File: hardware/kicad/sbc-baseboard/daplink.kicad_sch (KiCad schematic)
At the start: 15 parts, among them J601 SWD (K20), SW601 DAP RESET, U601 MK20DX128VFM5, Y601 8MHz

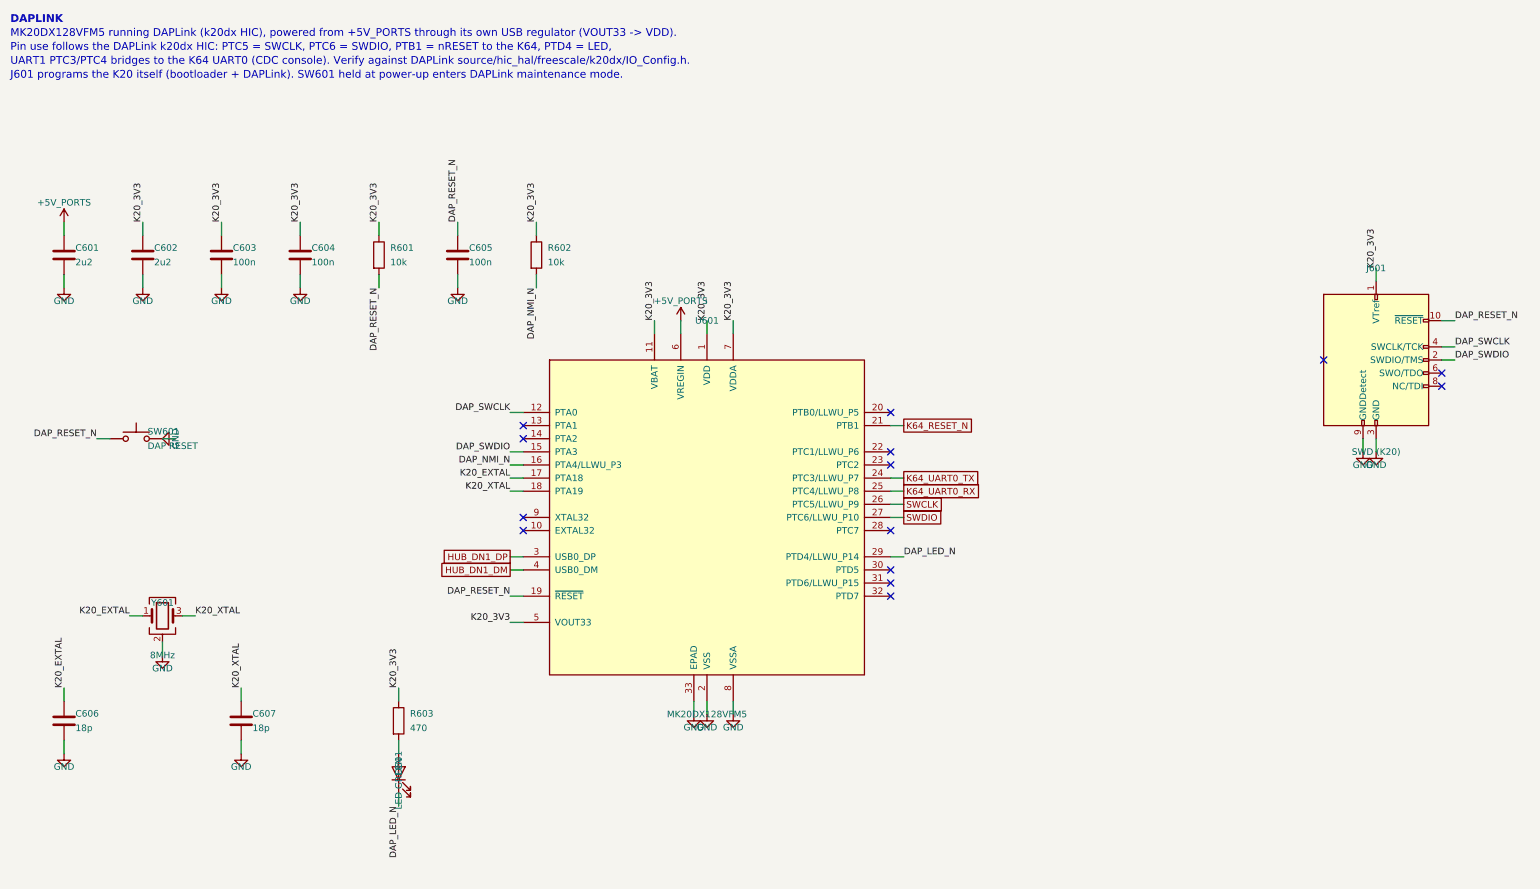
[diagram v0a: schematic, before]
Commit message: Re-lay out every sheet around its main component
Nets fan out of each hub IC as wires at pin pitch; connectors, series
parts, pull-ups and power symbols sit at the lane ends, and labels are
kept for nets that leave the page. Supply pins share a bus with their
decoupling; ESD arrays sit on the connector's D-/D+ rows and port
switches on the VBUS row, so every wire into a receptacle is straight;
the stacked USB-A is a two-unit symbol, one per port. Relays move to
their own sheet (8xx). ESD diodes use KiCad's PESD5V0S1UL in SOD-882.

Generator: gen/fanout.py (lane engine), gen/check_geom.py (endpoint
contacts), gen/netcheck.py (wire-level rail merges). ERC, both checks
and a renumbering-tolerant netlist diff against the first pass all
clean; 331 parts, 354 nets.

Co-Authored-By: Claude Fable 5.1 <noreply@anthropic.com>
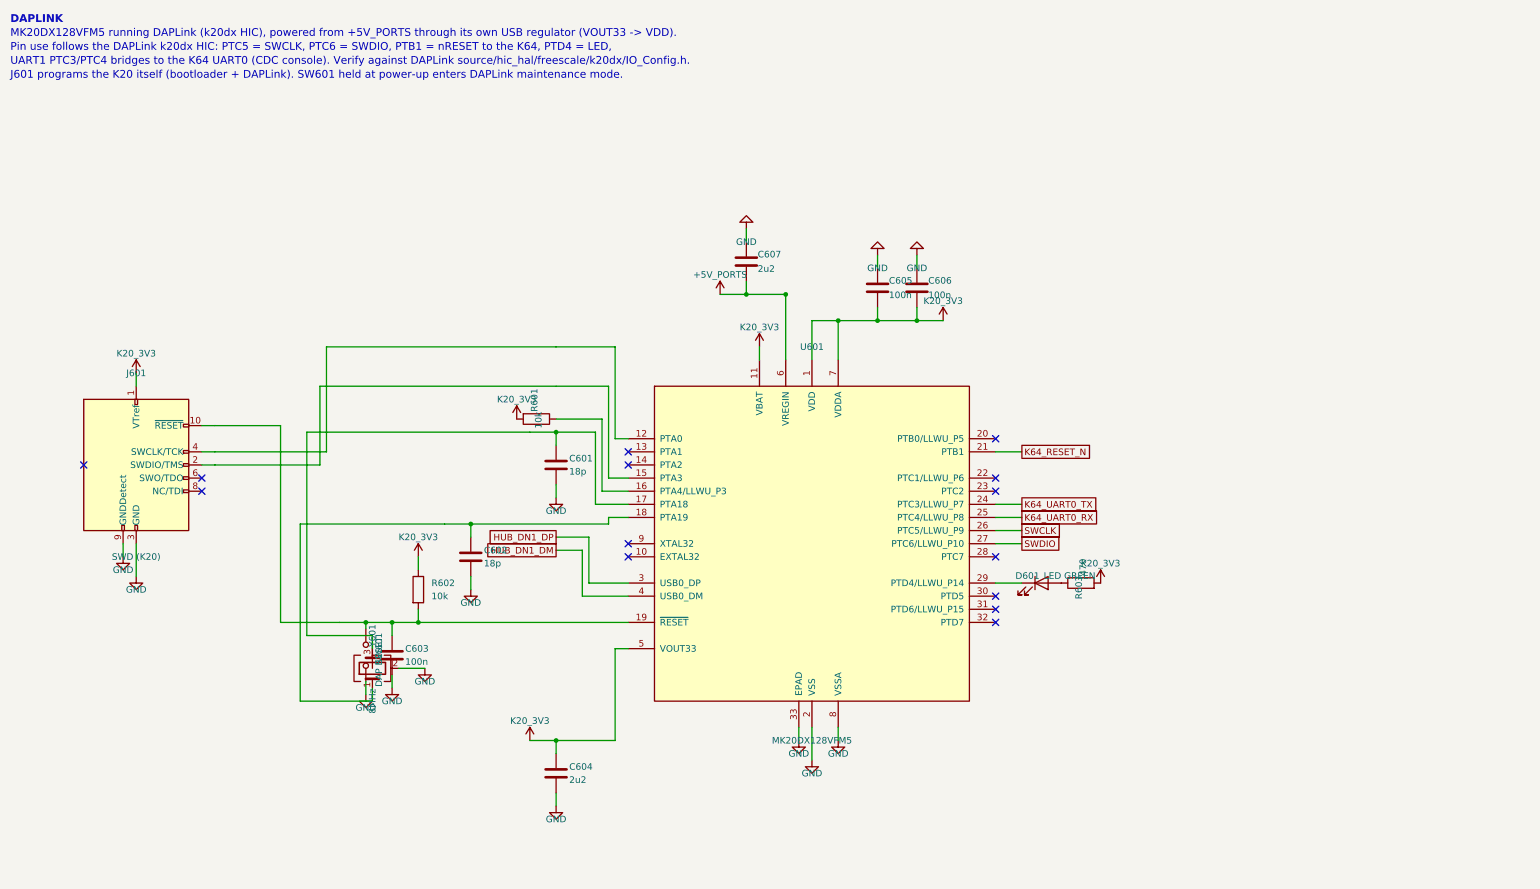
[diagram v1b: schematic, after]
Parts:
- C601, C602: value 2u2 -> 18p
- C604: value 100n -> 2u2
- C606: value 18p -> 100n
- C607: value 18p -> 2u2
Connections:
- net +5V_PORTS: now also C607.2; no longer C601.1
- net GND: now also C605.1, C606.1, C607.1; no longer C605.2, C606.2, C607.2
- net K20_3V3: now also C605.2, C606.2, R601.2, R603.2; no longer C602.1, C603.1, R601.1, R603.1
- net at D601.2 (A): now also R603.1; no longer R603.2
- net DAP_LED_N: no longer names the net of D601.1 (K), U601.29 (PTD4/LLWU_P14)
- net DAP_NMI_N: no longer names the net of R602.2
- net DAP_NMI_N: now also C603.1, J601.10 (~{RESET}), SW601.1, U601.19 (~{RESET}); no longer U601.16 (PTA4/LLWU_P3)
- removed net DAP_RESET_N: C605.1, J601.10 (~{RESET}), R601.2, SW601.1, U601.19 (~{RESET})
- net DAP_SWCLK: no longer names the net of J601.4 (SWCLK/TCK), U601.12 (PTA0)
- net DAP_SWDIO: no longer names the net of J601.2 (SWDIO/TMS), U601.15 (PTA3)
- removed net K20_EXTAL: C606.1, U601.17 (PTA18), Y601.1
- removed net K20_XTAL: C607.1, U601.18 (PTA19), Y601.3
- new net: C601.1, U601.17 (PTA18), Y601.3
- new net: R601.1, U601.16 (PTA4/LLWU_P3)
- new net: C602.1, U601.18 (PTA19), Y601.1

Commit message: Symbol direction, field text and decoupling ladders across every sheet
Every GND symbol now hangs down and every rail stands up: decoupling
hangs from the supply bus into a GND rail with one GND symbol at the end
(ladders), rails on crowded supply pins are jogged sideways, the SWD
header is mirrored instead of rotated. Field text on in-line parts reads
horizontally (KiCad adds the symbol rotation to the field angle) and is
placed by lane direction; hanging parts carry their text on the side away
from the pin; IC reference and value sit where the library put them.
Power sheet: bus buffer moved under the STUSB4500's I2C lanes with direct
routes, programmer by label, buck drawn as a box with its input and
output capacitors as ladders. New gen/check_layout.py reports text and
wire overlaps and wrong-way power symbols; PDF export draws hop-overs.

ERC 0, no merged rails, netlist equivalent; text-overlap residue listed
in the layout checker output remains on the hub, relays and DAPLink.

Co-Authored-By: Claude Fable 5.1 <noreply@anthropic.com>
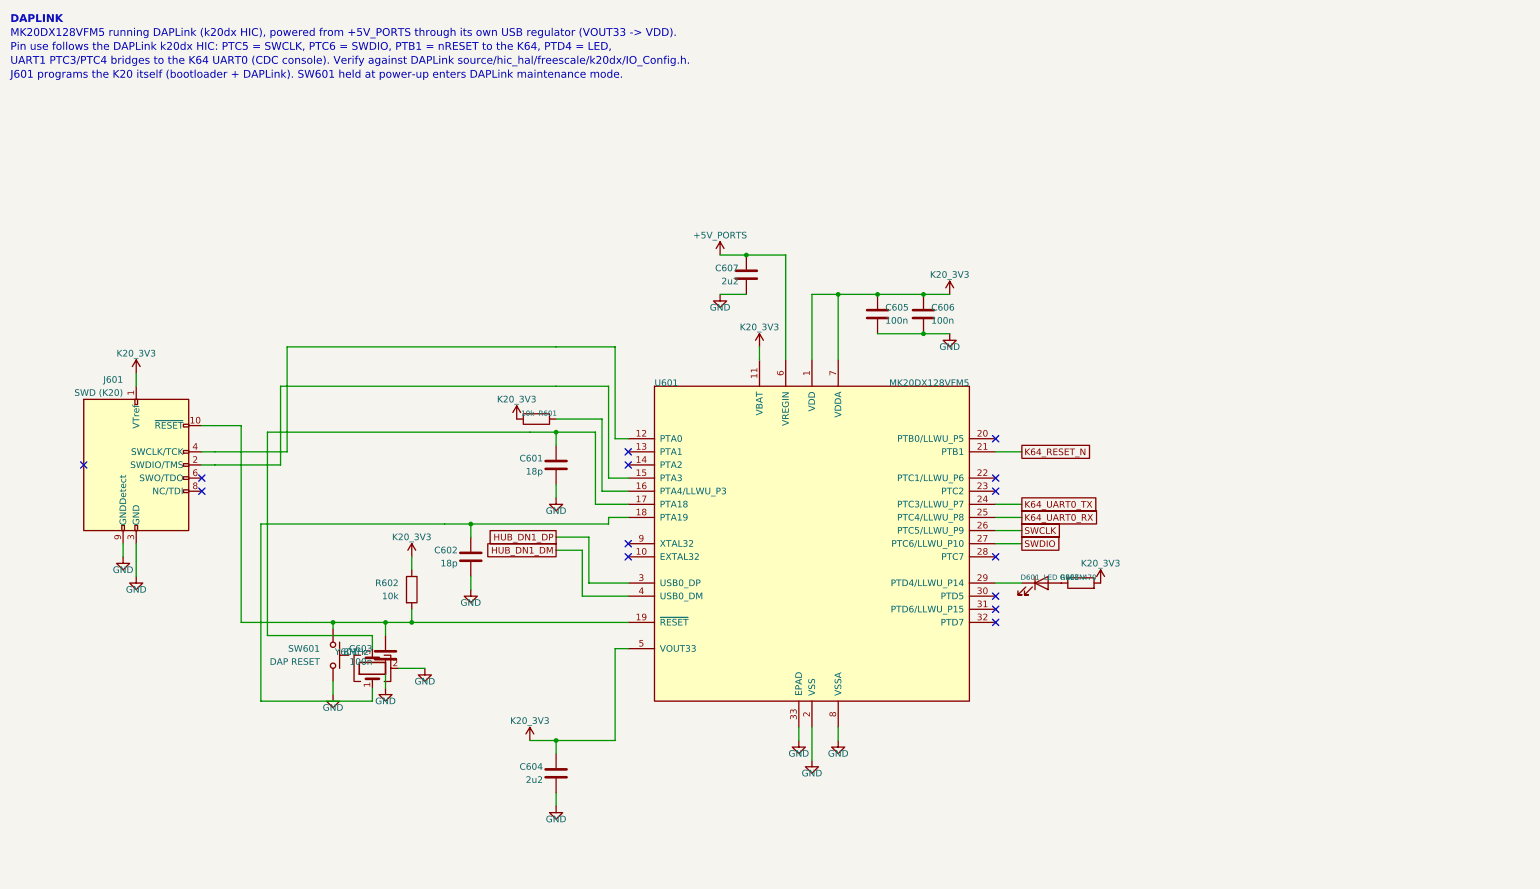
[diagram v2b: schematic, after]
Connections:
- net +5V_PORTS: now also C607.1; no longer C607.2
- net GND: now also C605.2, C606.2, C607.2; no longer C605.1, C606.1, C607.1
- net K20_3V3: now also C605.1, C606.1; no longer C605.2, C606.2

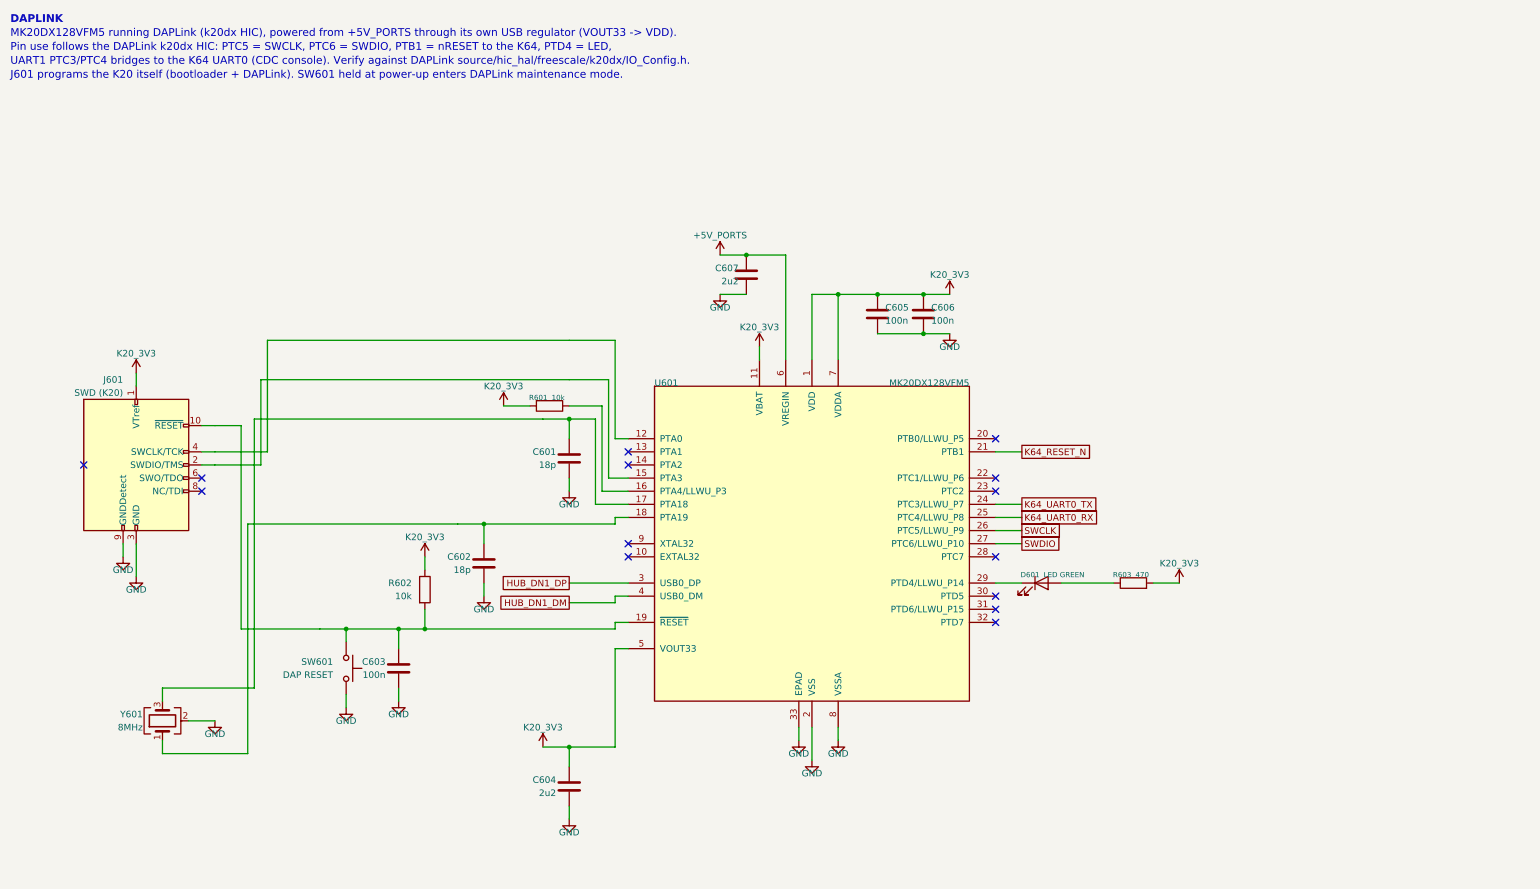
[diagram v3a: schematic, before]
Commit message: Symbol name clearance, divider at the reading pin, inlet TVS orientation
Symbols: a top or bottom pin's name runs vertically into the body, so box
symbols now grow outward by whole rows wherever such a name would reach a
side pin's name (USB2517 three rows on top, K64 two rows top and bottom,
PCA9517A three rows on top); the side-pin rows stay where they were so the
sheet layouts are unaffected. U402's VDD names no longer print over USBUP_DP.

Frame pass: nothing on the sheet frame or the title block, enforced by the
layout gate (usable area 15..405 x 15..282 mm, title block from 300/253).

Flow pass: pull-ups hang up to their rail, pull-downs hang down (R408/R409
and the other strap and sense resistors). The J1 VBUS_DET divider sits at
U402 pin 44, the pin that reads it; J1's VBUS lane is a plain stretch that
U401 taps; J1 and U401 lifted clear of the hub's +3V3 bus. The hub's left
strap lanes turn in columns starting at x = 118.11 so they clear the bottom
decoupling ladders (fan() grew a turn_at argument for this).

Inlet TVS D102 hangs from J2's VBUS lane as a D_Zener with its cathode on
VBUS_IN. At 8579cd2 it was drawn with the bidirectional D_TVS symbol and
pad 1 (the SMA cathode) on GND, which would have forward-biased it.

Bucks: the FB pulls start past the catch diode's text; the two notes are
rewrapped and sit between U101 and the compensation parts.

Gates on every sheet: ERC 0, endpoint contacts 0, rail merges 0, frame 0,
no text on bodies or wires. Connectivity identical to 8579cd2 (symmetric
passives order-free) except the TVS orientation.

Co-Authored-By: Claude Fable 5.1 <noreply@anthropic.com>
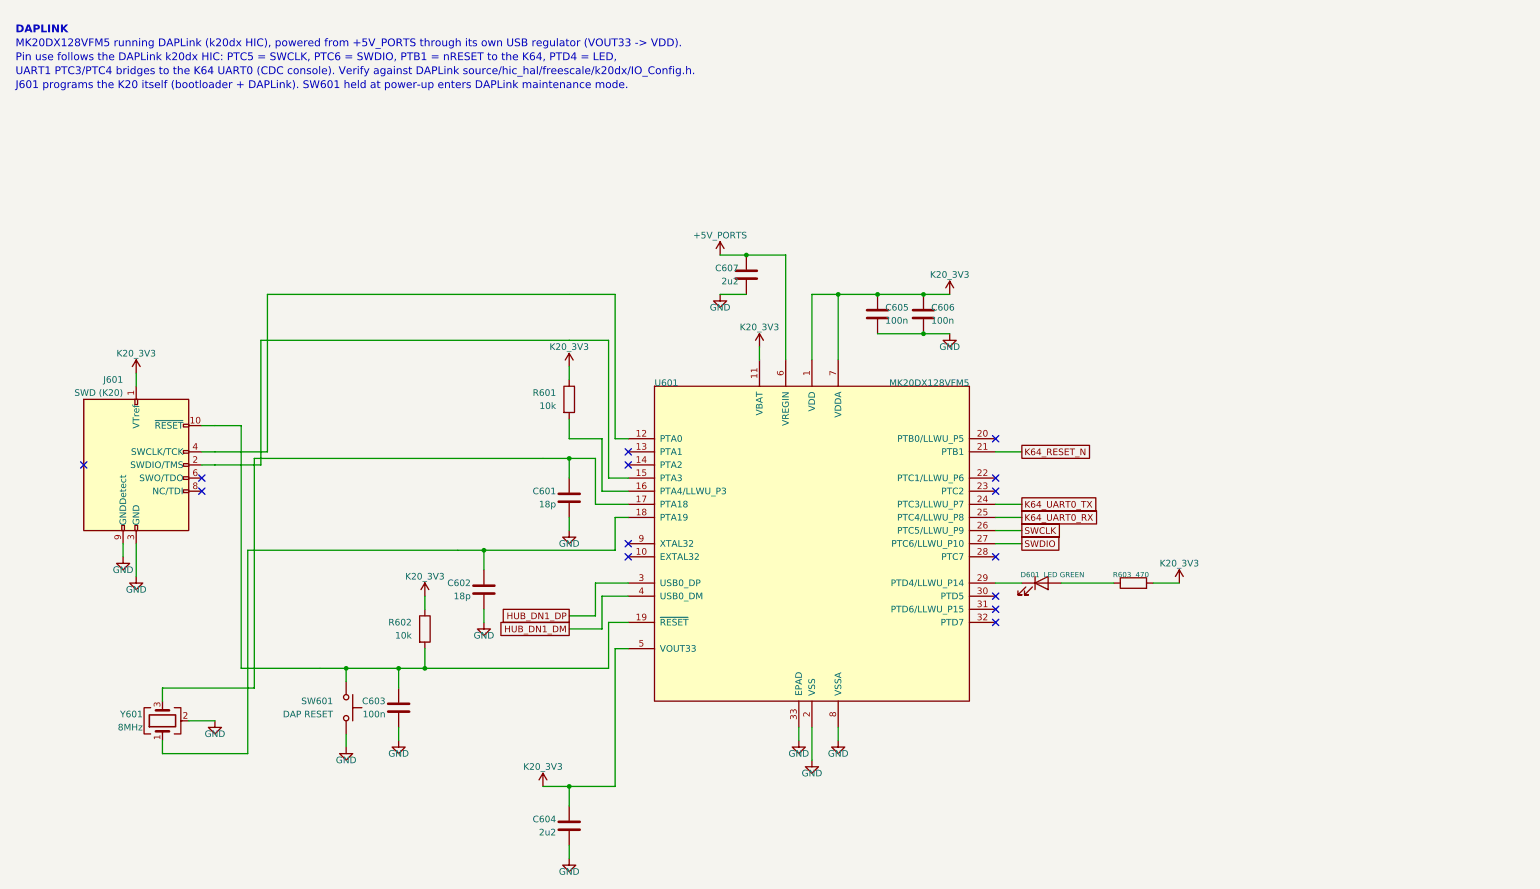
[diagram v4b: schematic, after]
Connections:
- net K20_3V3: now also R601.1; no longer R601.2
- net at U601.16 (PTA4/LLWU_P3): now also R601.2; no longer R601.1
